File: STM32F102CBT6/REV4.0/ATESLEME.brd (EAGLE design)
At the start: 35.3 x 57.9 mm, 68 parts, among them IC1 EN25F40-100GCP-TR, U1 ADXL345PATRICK, U2 MS561101BA03-50, U3 AMS1117-3.3, U4 STM32F102CBT6, U5 38kHz, U8 SI2308CDS-T1-GE3, U9 SI2308CDS-T1-GE3, X1 JST-XH-04-PIN-LONG-PAD, Y2 ABM2B-8.000MHZ-10-1-U-T

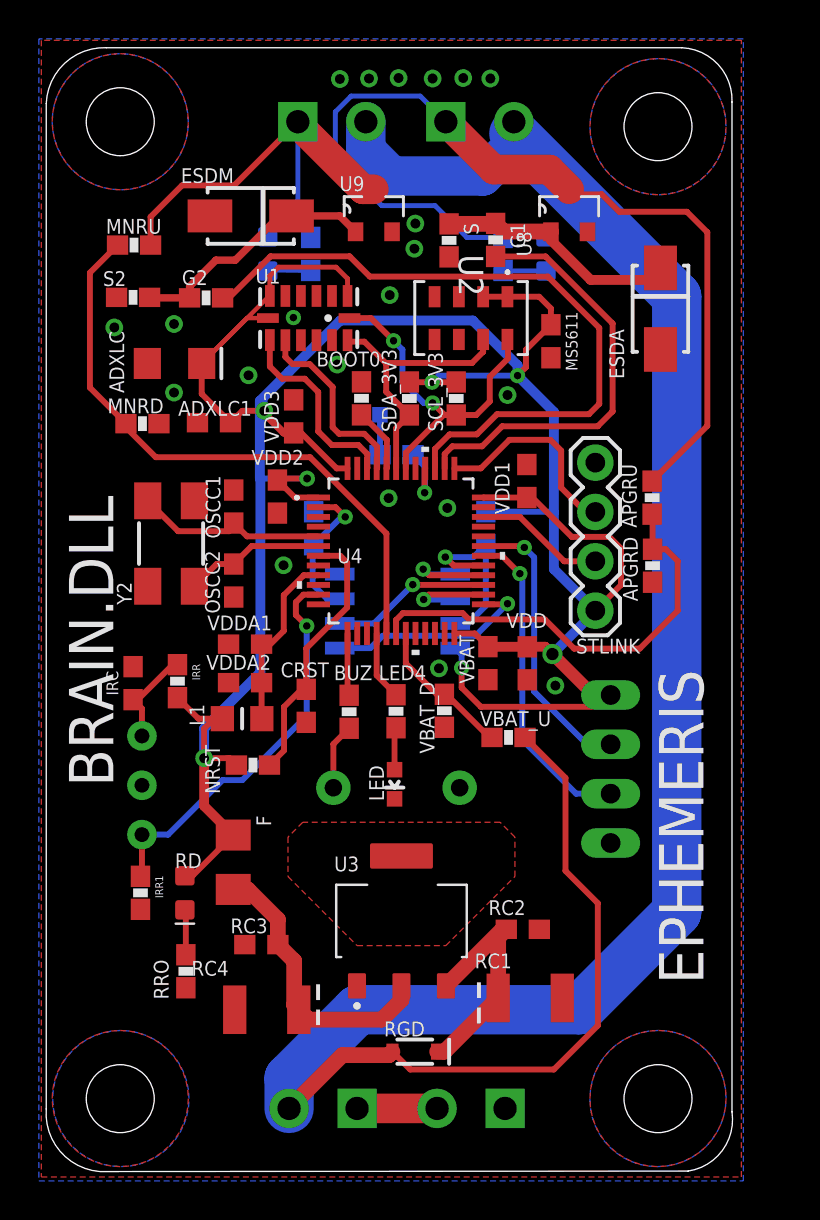
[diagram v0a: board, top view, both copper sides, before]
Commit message: Regulator was added for e match and released new two version for ordering
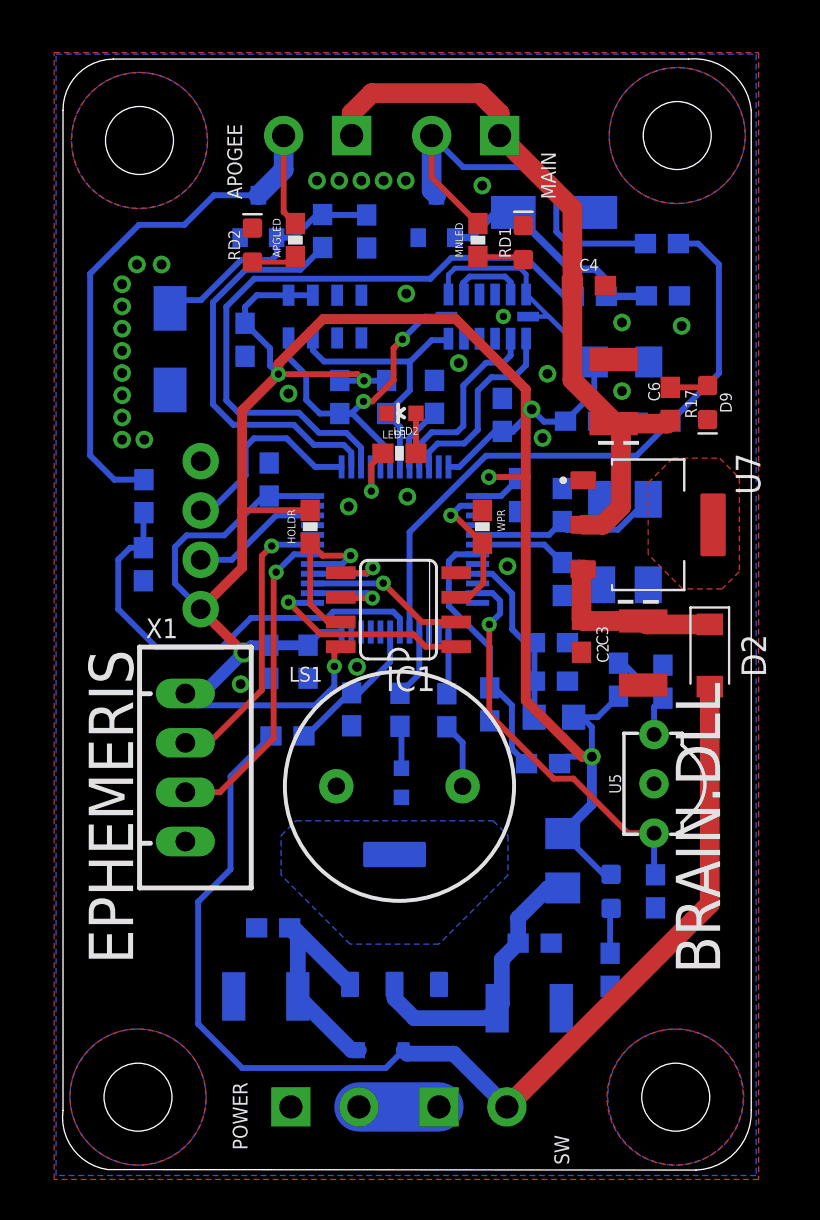
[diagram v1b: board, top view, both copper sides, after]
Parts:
- added C2, C6: 22uF, SparkFun-Capacitors:EIA3528
- added C3, C4: 100nF, SparkFun-Capacitors:0603
- added D2: B5819W, Diode:SODFL3718X115
- added D9: (no value), SparkFun-LED:LED-0603
- added R17: 1k5, SparkFun-Resistors:0603
- added U7: AMS1117-3.3, AMS1117-3.3:SOT229P700X180-4N
- moved IRC 27.3 mm to (32.1, 25.7), flipped to the bottom
- moved S2 27.3 mm to (32.1, 45.6), flipped to the bottom
- moved MNRU 27.2 mm to (32.1, 48.3), flipped to the bottom
- moved IRR1 26.5 mm to (31.8, 14.9), flipped to the bottom
- moved U5 26.4 mm to (31.7, 20.4), flipped to the top
- moved MNRD 26.3 mm to (31.6, 39.1), flipped to the bottom
- moved APGRD 26.2 mm to (5.38, 31.8), flipped to the bottom
- moved APGRU 26.2 mm to (5.41, 35.3), flipped to the bottom
- moved ESDA 25.3 mm to (6.76, 42.8), flipped to the bottom
- moved Y2 23.4 mm to (30.2, 32.9), flipped to the bottom
- moved ADXLC 23.0 mm to (30.0, 42.2), flipped to the bottom
- moved IRR 22.7 mm to (29.8, 25.8), flipped to the bottom
- moved RD 21.9 mm to (29.5, 14.9), flipped to the bottom
- moved X1 21.9 mm to (7.54, 21.3), flipped to the top
- moved RRO 21.8 mm to (29.4, 10.9), flipped to the bottom
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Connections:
- net VCC renamed N$9
- new net 5V: APOGEE.1, C4.1, C6.A, MAIN.1, R17.2, U7.2
- new net HT1: U7.4
- new net N$11: D9.A, R17.1
- new net N$7: C2.A, C3.1, D2.1, U7.3
- net GND: now also C2.C, C3.2, C4.2, C6.C, D9.C, U7.1
- net VAPG: now also APOGEE.2; no longer APOGEE.1
- net VIN: now also D2.2; no longer APOGEE.2, MAIN.2
- net VMN: now also MAIN.2; no longer MAIN.1
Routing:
- net VIN: track 115.5 -> 60.8 mm
- net 5V: track 0.00 -> 37.8 mm
- net VAPG: track 49.1 -> 31.4 mm
- net N$7: track 0.00 -> 9.32 mm
- net GND: track 0.00 -> 3.95 mm, vias 21 -> 31
- net MN: track 36.1 -> 33.5 mm
- net 3.3V: track 154.3 -> 151.8 mm
- net N$11: track 0.00 -> 1.96 mm
- net APG: track 22.3 -> 21.0 mm
- net VMNS: track 31.6 -> 32.6 mm
- added copper zone on layer 16, net HT
- added copper zone on layer 1, net HT1
- removed copper zone on layer 1, net HT
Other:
- board size 35.3 x 57.9 mm -> 35.5 x 57.2 mm

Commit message: Sotware and Algorithm was added
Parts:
- U7: value AMS1117-3.3 -> AMS1117-5.0
- moved D9 8.77 mm to (30.9, 48.1), turned to 180 degrees
- moved C4 7.27 mm to (29.8, 39.0)
- moved R17 6.56 mm to (30.9, 46.4), turned to 180 degrees
- moved C6 1.55 mm to (29.8, 42.2), turned to 180 degrees
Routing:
- net 5V: track 37.8 -> 36.6 mm
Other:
- board text added: "3.3"
- board text added: "CLK"
- board text added: "GND"
- board text added: "IO"
- board text added: "RX1"
- board text added: "TX1"
